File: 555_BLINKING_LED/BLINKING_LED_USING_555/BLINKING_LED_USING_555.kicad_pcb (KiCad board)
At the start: 2 copper layers, 39.8 x 23.2 mm, 14 parts, among them U1 ICM7555xB, U2 ICM7555xB

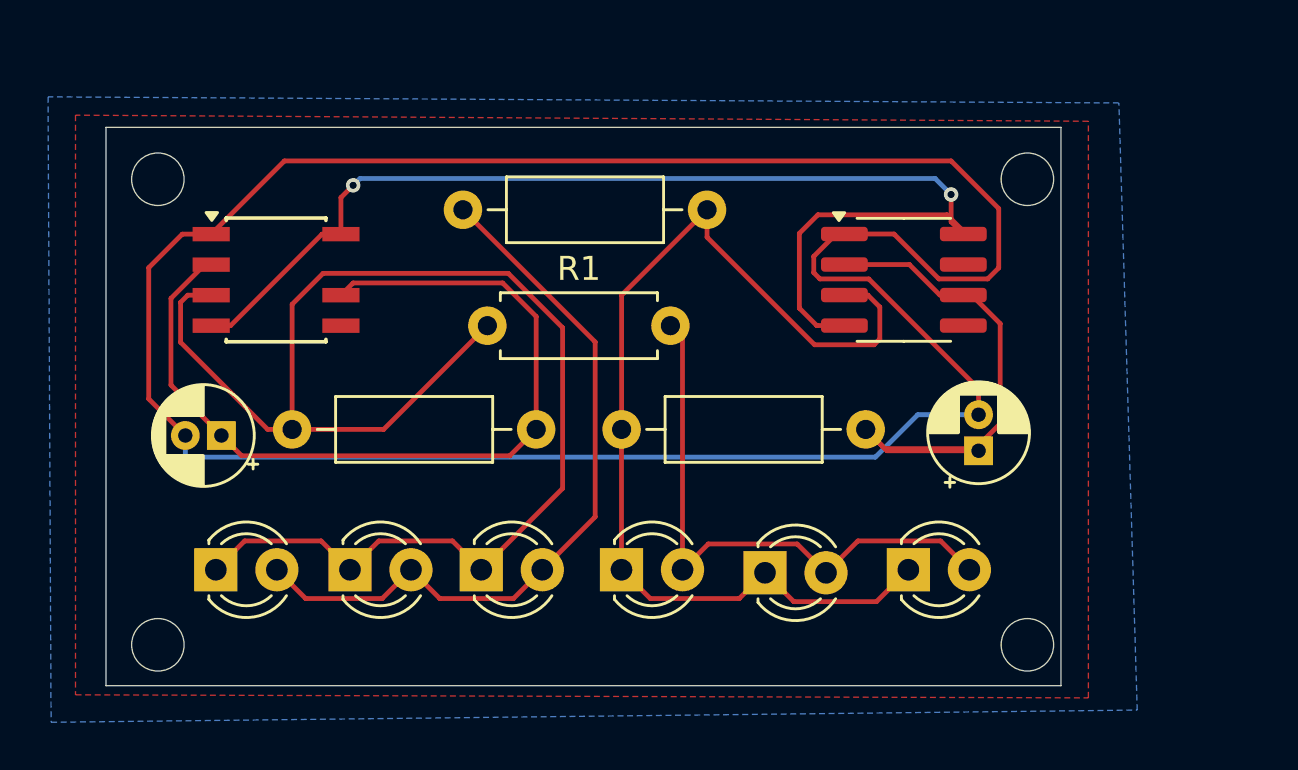
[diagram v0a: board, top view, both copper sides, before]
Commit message: temp sensor module refined and audio amplifier made
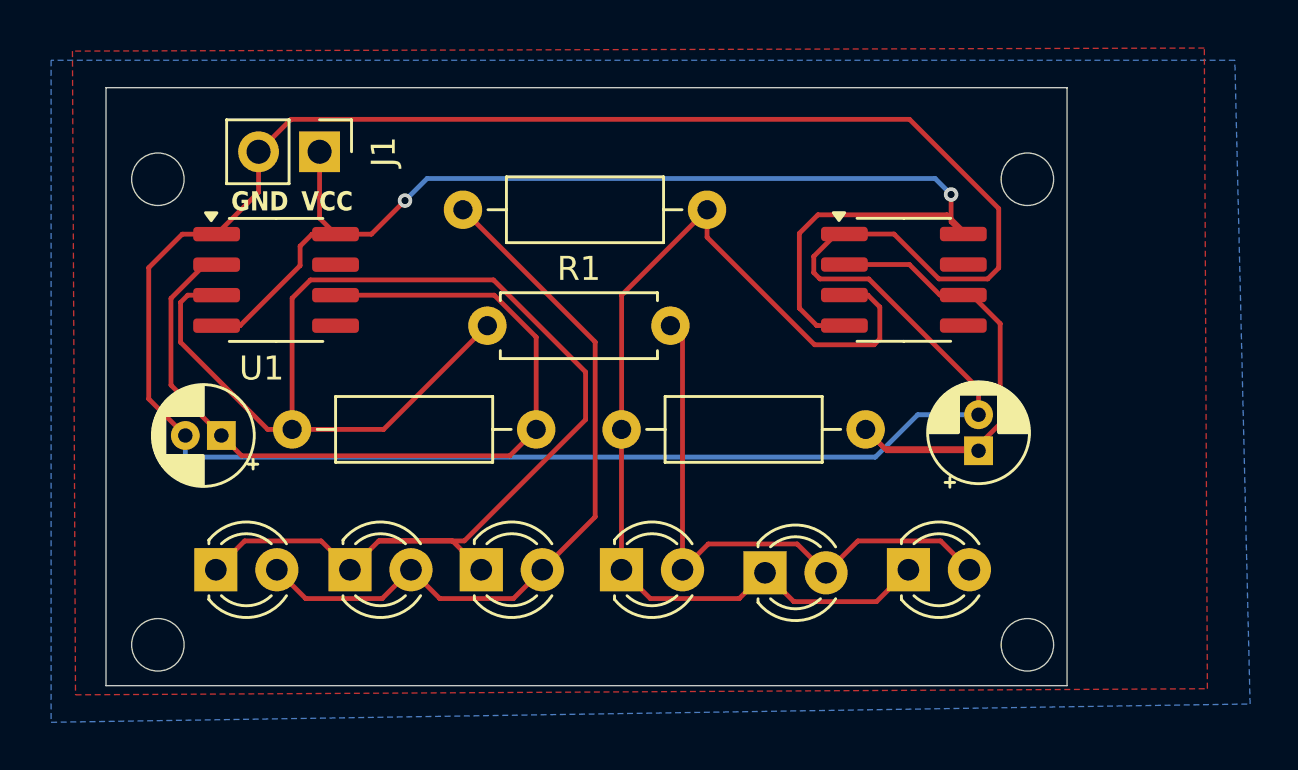
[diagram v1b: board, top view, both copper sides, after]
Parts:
- added J1: Conn_01x02_Socket, Connector_PinHeader_2.54mm:PinHeader_1x02_P2.54mm_Vertical, F.Cu at (140.1, 58.2)
- U1: footprint Package_SO:SOIC-8-N7_3.9x4.9mm_P1.27mm -> Package_SO:SOIC-8_3.9x4.9mm_P1.27mm
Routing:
- net +5V: track 49.2 -> 53.6 mm
- net /Q_1: track 61.6 -> 64.4 mm
- net GND: track 102.4 -> 104.8 mm
- net /THR_1: track 36.4 -> 35.7 mm
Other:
- board size 39.8 x 23.2 mm -> 40 x 24.9 mm
- board text added: "GND"
- board text added: "VCC"
